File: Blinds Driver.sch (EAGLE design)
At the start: 29 parts

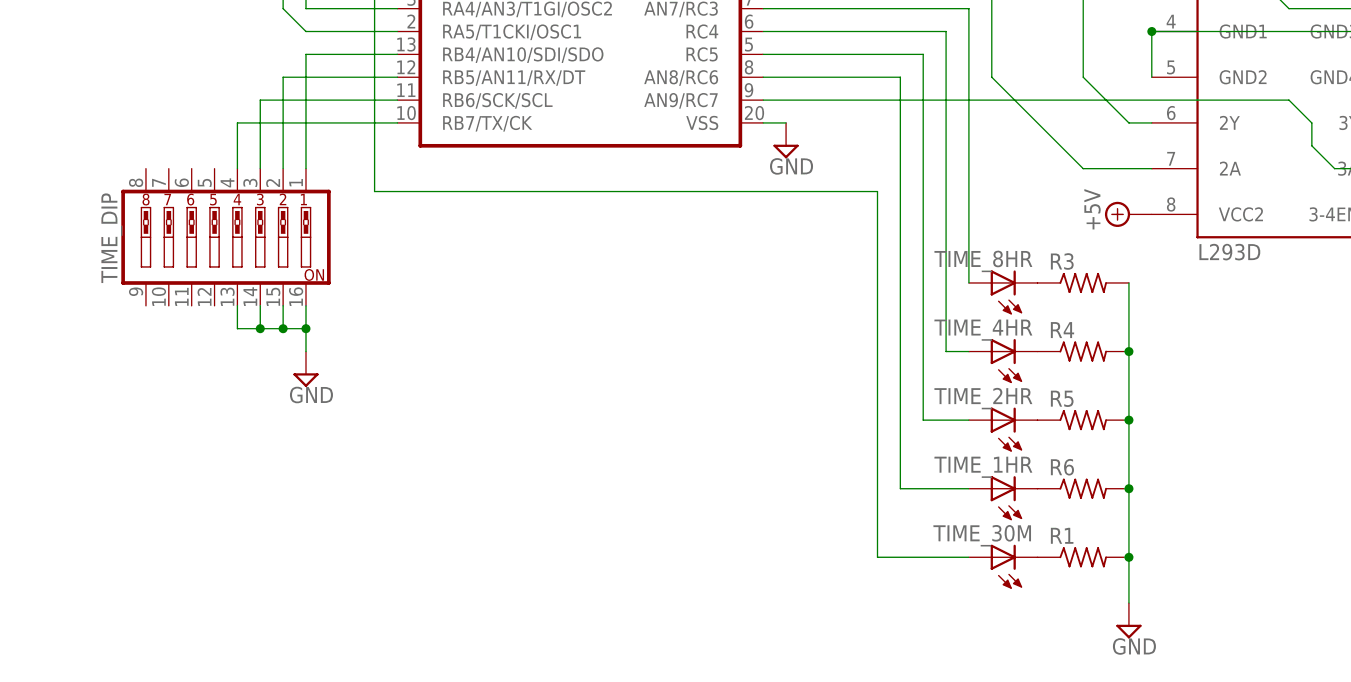
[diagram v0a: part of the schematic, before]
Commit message: Fit into smaller PCB! Use 4-pin DIP
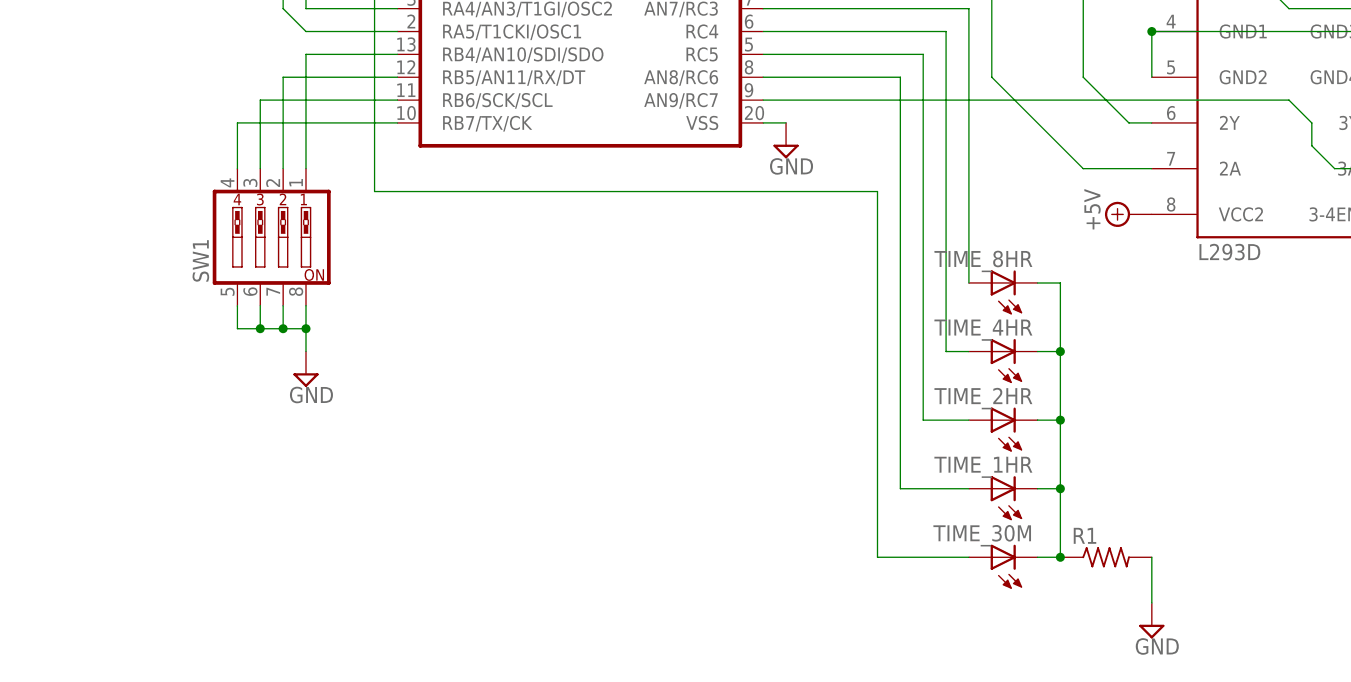
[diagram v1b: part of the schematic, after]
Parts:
- removed R3, R4, R5, R6: (no value), resistor:R-US_0207/10
- removed TIME_DIP: (no value), special:SW_DIP-8
- added SW1: (no value), special:SW_DIP-4
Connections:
- removed net N$15: R4.1, TIME_4HR.C
- removed net N$16: R5.1, TIME_2HR.C
- removed net N$17: R6.1, TIME_1HR.C
- removed net N$23: R1.1, TIME_30M.C
- net GND: now also SW1.5, SW1.6, SW1.7, SW1.8; no longer R3.2, R4.2, R5.2, R6.2, TIME_DIP.13, TIME_DIP.14, TIME_DIP.15, TIME_DIP.16
- net N$14: now also R1.1, TIME_1HR.C, TIME_2HR.C, TIME_30M.C, TIME_4HR.C; no longer R3.1
- net N$4: now also SW1.1; no longer TIME_DIP.1
- net N$5: now also SW1.2; no longer TIME_DIP.2
- net N$7: now also SW1.3; no longer TIME_DIP.3
- net N$9: now also SW1.4; no longer TIME_DIP.4
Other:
- moved on the sheet: R1
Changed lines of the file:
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@@
 <part name="TIME_2HR" library="led" deviceset="LED" device="5MM"/>
 <part name="TIME_1HR" library="led" deviceset="LED" device="5MM"/>
-<part name="R3" library="resistor" deviceset="R-US_" device="0207/10"/>
-<part name="R4" library="resistor" deviceset="R-US_" device="0207/10"/>
-<part name="R5" library="resistor" deviceset="R-US_" device="0207/10"/>
-<part name="R6" library="resistor" deviceset="R-US_" device="0207/10"/>
 <part name="R7" library="resistor" deviceset="R-US_" device="0207/10"/>
 <part name="R8" library="resistor" deviceset="R-US_" device="0207/10"/>
@@
 <part name="TIME_30M" library="led" deviceset="LED" device="5MM"/>
 <part name="R1" library="resistor" deviceset="R-US_" device="0207/10"/>
-<part name="TIME_DIP" library="special" deviceset="SW_DIP-8" device=""/>
 <part name="SUPPLY12" library="supply2" deviceset="GND" device=""/>
 <part name="D1" library="diode" deviceset="1N4004" device=""/>
@@
 <part name="SUPPLY21" library="supply2" deviceset="+12V" device=""/>
 <part name="MOTOR_OUT" library="linear" deviceset="78*" device="T" technology="05"/>
+<part name="SW1" library="special" deviceset="SW_DIP-4" device=""/>
 </parts>
 <sheets>
@@
 <instance part="TIME_2HR" gate="G$1" x="25.4" y="17.78" rot="R90"/>
 <instance part="TIME_1HR" gate="G$1" x="25.4" y="10.16" rot="R90"/>
-<instance part="R3" gate="G$1" x="35.56" y="33.02"/>
-<instance part="R4" gate="G$1" x="35.56" y="25.4"/>
-<instance part="R5" gate="G$1" x="35.56" y="17.78"/>
-<instance part="R6" gate="G$1" x="35.56" y="10.16"/>
 <instance part="R7" gate="G$1" x="73.66" y="33.02" rot="R270"/>
 <instance part="R8" gate="G$1" x="38.1" y="78.74"/>
-<instance part="SUPPLY11" gate="GND" x="40.64" y="-5.08"/>
+<instance part="SUPPLY11" gate="GND" x="43.18" y="-5.08"/>
 <instance part="ADDSMALLTIME" gate="1" x="-66.04" y="116.84" rot="R270"/>
 <instance part="ADDLARGETIME" gate="1" x="-66.04" y="104.14" rot="R270"/>
@@
 <instance part="SUPPLY13" gate="GND" x="-78.74" y="116.84" rot="R270"/>
 <instance part="TIME_30M" gate="G$1" x="25.4" y="2.54" rot="R90"/>
-<instance part="R1" gate="G$1" x="35.56" y="2.54"/>
-<instance part="TIME_DIP" gate="A" x="-60.96" y="38.1" rot="R90"/>
+<instance part="R1" gate="G$1" x="38.1" y="2.54"/>
 <instance part="SUPPLY12" gate="GND" x="-50.8" y="22.86"/>
 <instance part="D1" gate="1" x="99.06" y="76.2" rot="R270"/>
@@
 <instance part="SUPPLY21" gate="+12V" x="116.84" y="27.94" rot="R180"/>
 <instance part="MOTOR_OUT" gate="A1" x="137.16" y="55.88" rot="R90"/>
+<instance part="SW1" gate="A" x="-55.88" y="38.1" rot="R90"/>
 </instances>
 <busses>
@@
 </segment>
 <segment>
-<pinref part="R3" gate="G$1" pin="2"/>
-<pinref part="R4" gate="G$1" pin="2"/>
-<wire x1="40.64" y1="33.02" x2="40.64" y2="25.4" width="0.1524" layer="91"/>
-<pinref part="R5" gate="G$1" pin="2"/>
-<wire x1="40.64" y1="25.4" x2="40.64" y2="17.78" width="0.1524" layer="91"/>
-<pinref part="R6" gate="G$1" pin="2"/>
-<wire x1="40.64" y1="17.78" x2="40.64" y2="10.16" width="0.1524" layer="91"/>
-<wire x1="40.64" y1="10.16" x2="40.64" y2="2.54" width="0.1524" layer="91"/>
 <pinref part="SUPPLY11" gate="GND" pin="GND"/>
 <pinref part="R1" gate="G$1" pin="2"/>
-<wire x1="40.64" y1="2.54" x2="40.64" y2="-2.54" width="0.1524" layer="91"/>
-<junction x="40.64" y="2.54"/>
-<junction x="40.64" y="10.16"/>
-<junction x="40.64" y="17.78"/>
-<junction x="40.64" y="25.4"/>
+<wire x1="43.18" y1="2.54" x2="43.18" y2="-2.54" width="0.1524" layer="91"/>
 </segment>
 <segment>
@@
 <segment>
 <pinref part="SUPPLY12" gate="GND" pin="GND"/>
-<pinref part="TIME_DIP" gate="A" pin="16"/>
 <wire x1="-50.8" y1="25.4" x2="-50.8" y2="27.94" width="0.1524" layer="91"/>
-<pinref part="TIME_DIP" gate="A" pin="15"/>
 <wire x1="-50.8" y1="27.94" x2="-50.8" y2="30.48" width="0.1524" layer="91"/>
 <wire x1="-53.34" y1="30.48" x2="-53.34" y2="27.94" width="0.1524" layer="91"/>
 <wire x1="-53.34" y1="27.94" x2="-50.8" y2="27.94" width="0.1524" layer="91"/>
-<pinref part="TIME_DIP" gate="A" pin="14"/>
 <wire x1="-55.88" y1="30.48" x2="-55.88" y2="27.94" width="0.1524" layer="91"/>
 <wire x1="-55.88" y1="27.94" x2="-53.34" y2="27.94" width="0.1524" layer="91"/>
-<pinref part="TIME_DIP" gate="A" pin="13"/>
 <wire x1="-58.42" y1="30.48" x2="-58.42" y2="27.94" width="0.1524" layer="91"/>
 <wire x1="-58.42" y1="27.94" x2="-55.88" y2="27.94" width="0.1524" layer="91"/>
@@
 <junction x="-53.34" y="27.94"/>
 <junction x="-55.88" y="27.94"/>
+<pinref part="SW1" gate="A" pin="5"/>
+<pinref part="SW1" gate="A" pin="6"/>
+<pinref part="SW1" gate="A" pin="7"/>
+<pinref part="SW1" gate="A" pin="8"/>
 </segment>
 <segment>
@@
 <pinref part="TIME_1HR" gate="G$1" pin="A"/>
 <wire x1="15.24" y1="10.16" x2="22.86" y2="10.16" width="0.1524" layer="91"/>
-</segment>
-</net>
-<net name="N$14" class="0">
-<segment>
-<pinref part="TIME_8HR" gate="G$1" pin="C"/>
-<pinref part="R3" gate="G$1" pin="1"/>
-</segment>
-</net>
-<net name="N$15" class="0">
-<segment>
-<pinref part="TIME_4HR" gate="G$1" pin="C"/>
-<pinref part="R4" gate="G$1" pin="1"/>
-</segment>
-</net>
-<net name="N$16" class="0">
-<segment>
-<pinref part="TIME_2HR" gate="G$1" pin="C"/>
-<pinref part="R5" gate="G$1" pin="1"/>
-</segment>
-</net>
-<net name="N$17" class="0">
-<segment>
-<pinref part="TIME_1HR" gate="G$1" pin="C"/>
-<pinref part="R6" gate="G$1" pin="1"/>
 </segment>
 </net>
@@
 </segment>
 </net>
-<net name="N$23" class="0">
-<segment>
-<pinref part="TIME_30M" gate="G$1" pin="C"/>
-<pinref part="R1" gate="G$1" pin="1"/>
-</segment>
-</net>
 <net name="N$24" class="0">
 <segment>
@@
 <net name="N$4" class="0">
 <segment>
-<pinref part="TIME_DIP" gate="A" pin="1"/>
 <wire x1="-50.8" y1="45.72" x2="-50.8" y2="58.42" width="0.1524" layer="91"/>
 <pinref part="CONTROLLER" gate="G$1" pin="RB4/AN10/SDI/SDO"/>
 <wire x1="-50.8" y1="58.42" x2="-40.64" y2="58.42" width="0.1524" layer="91"/>
+<pinref part="SW1" gate="A" pin="1"/>
 </segment>
 </net>
@@
 <pinref part="CONTROLLER" gate="G$1" pin="RB5/AN11/RX/DT"/>
 <wire x1="-40.64" y1="55.88" x2="-53.34" y2="55.88" width="0.1524" layer="91"/>
-<pinref part="TIME_DIP" gate="A" pin="2"/>
 <wire x1="-53.34" y1="55.88" x2="-53.34" y2="45.72" width="0.1524" layer="91"/>
+<pinref part="SW1" gate="A" pin="2"/>
 </segment>
 </net>
@@
 <pinref part="CONTROLLER" gate="G$1" pin="RB6/SCK/SCL"/>
 <wire x1="-40.64" y1="53.34" x2="-55.88" y2="53.34" width="0.1524" layer="91"/>
-<pinref part="TIME_DIP" gate="A" pin="3"/>
 <wire x1="-55.88" y1="53.34" x2="-55.88" y2="45.72" width="0.1524" layer="91"/>
+<pinref part="SW1" gate="A" pin="3"/>
 </segment>
 </net>
@@
 <pinref part="CONTROLLER" gate="G$1" pin="RB7/TX/CK"/>
 <wire x1="-40.64" y1="50.8" x2="-58.42" y2="50.8" width="0.1524" layer="91"/>
-<pinref part="TIME_DIP" gate="A" pin="4"/>
 <wire x1="-58.42" y1="50.8" x2="-58.42" y2="45.72" width="0.1524" layer="91"/>
+<pinref part="SW1" gate="A" pin="4"/>
 </segment>
 </net>
@@
 </segment>
 </net>
+<net name="N$14" class="0">
+<segment>
+<pinref part="TIME_8HR" gate="G$1" pin="C"/>
+<wire x1="30.48" y1="33.02" x2="33.02" y2="33.02" width="0.1524" layer="91"/>
+<wire x1="33.02" y1="33.02" x2="33.02" y2="25.4" width="0.1524" layer="91"/>
+<pinref part="TIME_30M" gate="G$1" pin="C"/>
+<pinref part="R1" gate="G$1" pin="1"/>
+<wire x1="33.02" y1="25.4" x2="33.02" y2="17.78" width="0.1524" layer="91"/>
+<wire x1="33.02" y1="17.78" x2="33.02" y2="10.16" width="0.1524" layer="91"/>
+<wire x1="33.02" y1="10.16" x2="33.02" y2="2.54" width="0.1524" layer="91"/>
+<wire x1="33.02" y1="2.54" x2="30.48" y2="2.54" width="0.1524" layer="91"/>
+<pinref part="TIME_1HR" gate="G$1" pin="C"/>
+<wire x1="30.48" y1="10.16" x2="33.02" y2="10.16" width="0.1524" layer="91"/>
+<pinref part="TIME_2HR" gate="G$1" pin="C"/>
+<wire x1="30.48" y1="17.78" x2="33.02" y2="17.78" width="0.1524" layer="91"/>
+<pinref part="TIME_4HR" gate="G$1" pin="C"/>
+<wire x1="30.48" y1="25.4" x2="33.02" y2="25.4" width="0.1524" layer="91"/>
+<junction x="33.02" y="25.4"/>
+<junction x="33.02" y="17.78"/>
+<junction x="33.02" y="10.16"/>
+<junction x="33.02" y="2.54"/>
+</segment>
+</net>

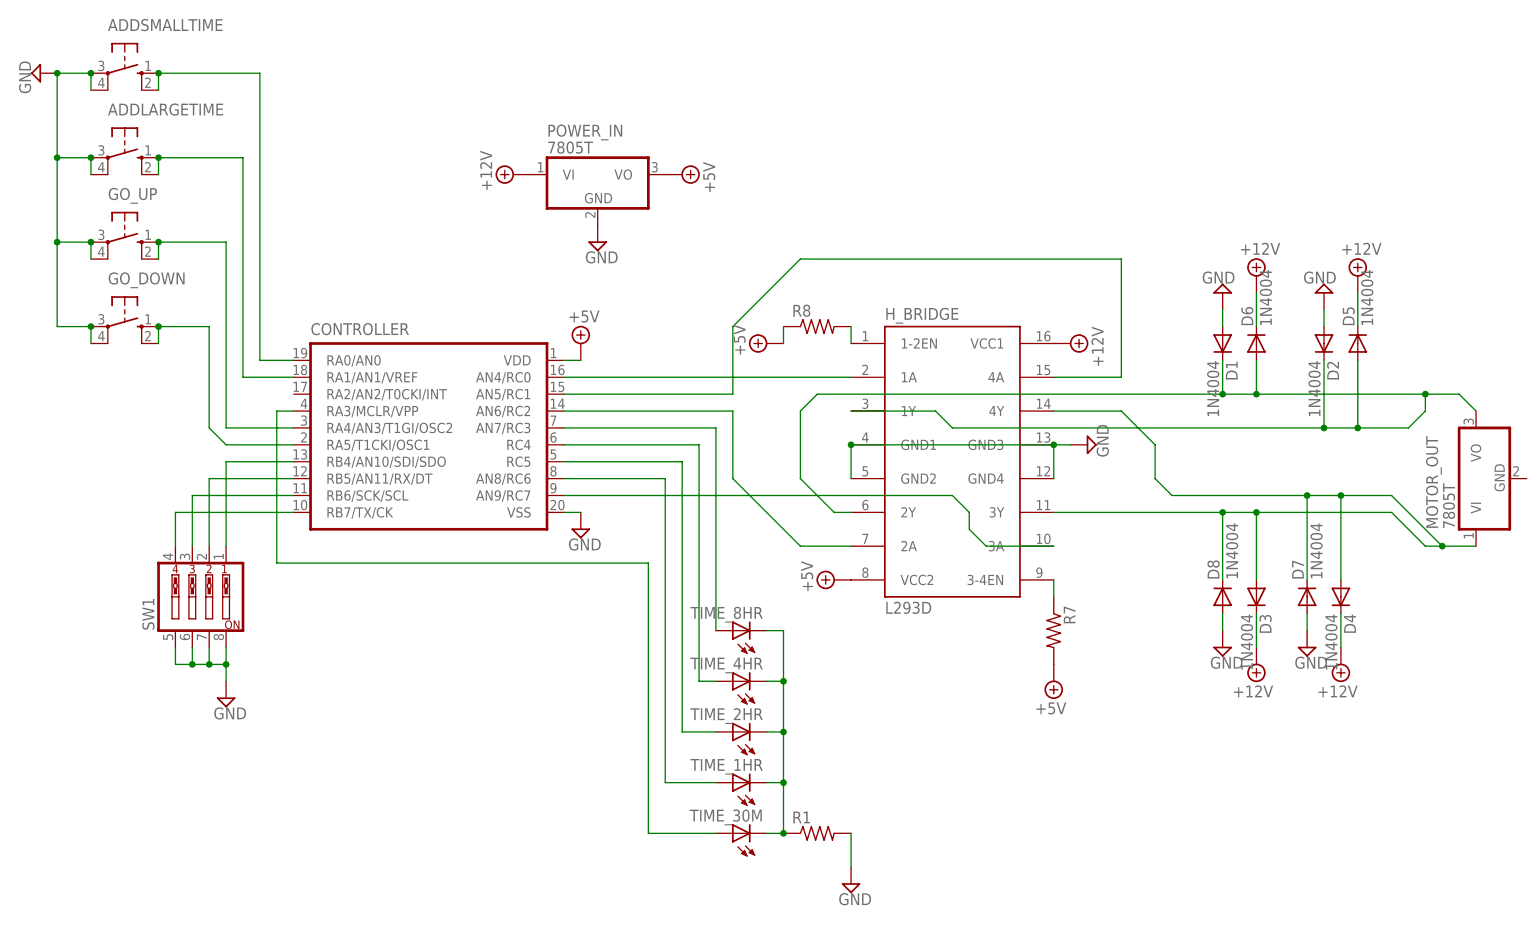
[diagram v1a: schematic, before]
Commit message: 1) Diodes were doubled up 2) Only one half-bridge is needed 3) VCC 2 is +12V, VCC1 is +5V 4) Added 2 bypass capacitors on the power supply lines to stabilize power supply
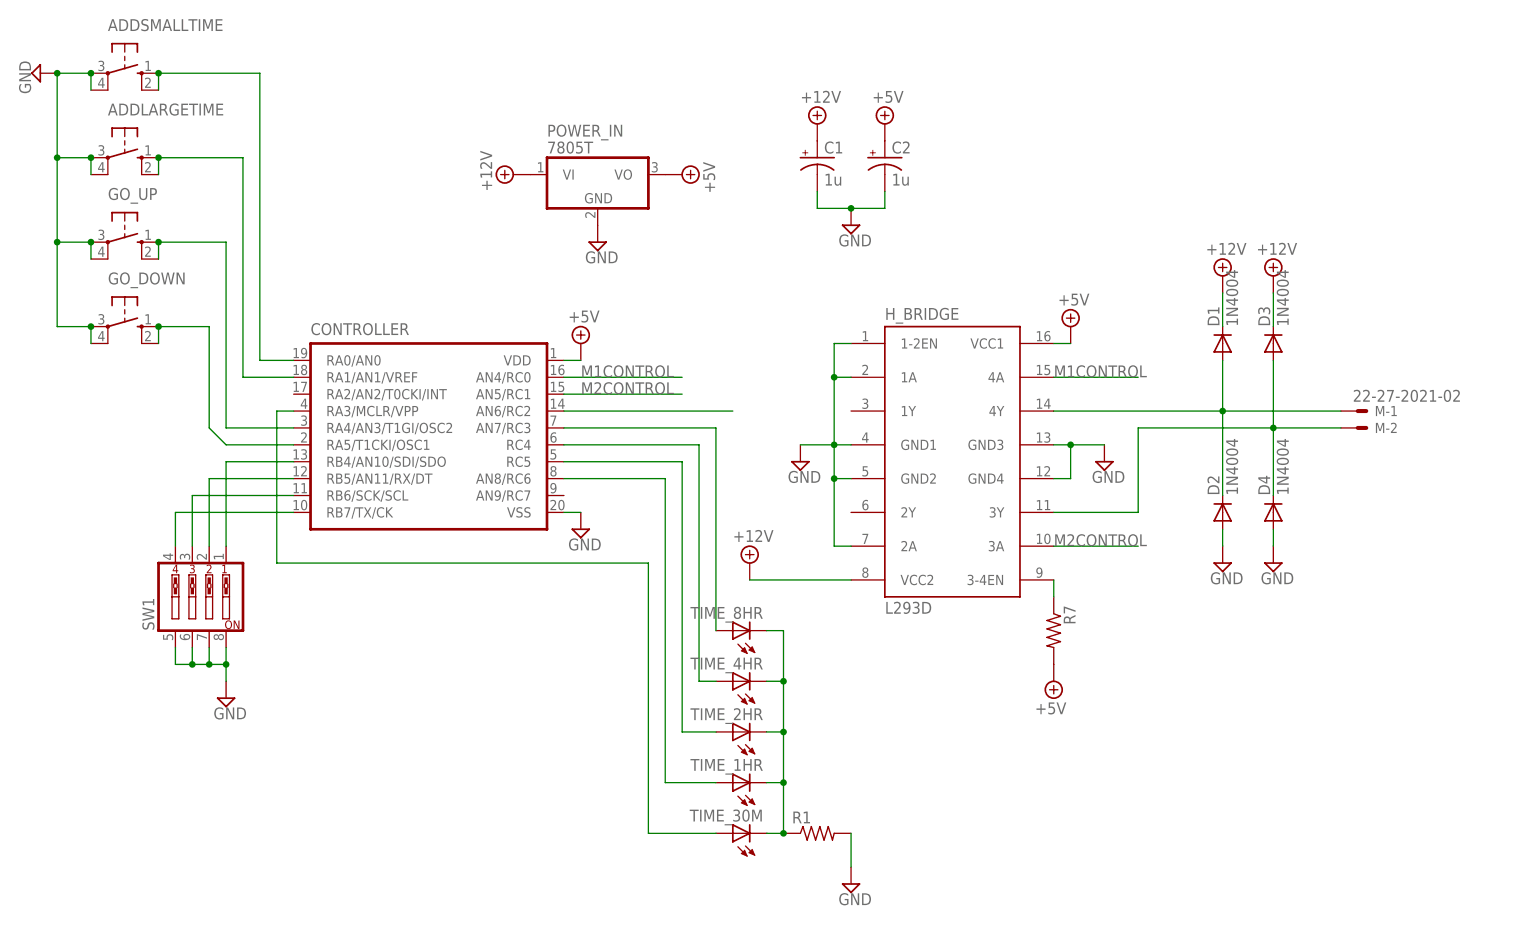
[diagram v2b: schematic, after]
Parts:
- removed D5, D6, D7, D8: 1N4004, diode:1N4004
- removed MOTOR_OUT: 7805T, linear:7805T
- removed R8: (no value), resistor:R-US_0207/10
- added C1, C2: 1u, rcl:CPOL-USE2,5-6E
- added M: 22-27-2021-02, con-molex:22-27-2021-02
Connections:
- removed net N$1: CONTROLLER.AN4/RC0, H_BRIDGE.1A
- removed net N$22: CONTROLLER.AN9/RC7, H_BRIDGE.3A
- removed net N$25: D1.C, D2.C, D5.A, D6.A, H_BRIDGE.1Y, H_BRIDGE.2Y, MOTOR_OUT.VO
- removed net N$28: D3.A, D4.A, D7.C, D8.C, H_BRIDGE.3Y, H_BRIDGE.4Y, MOTOR_OUT.VI
- new net M1CONTROL: CONTROLLER.AN4/RC0, H_BRIDGE.4A
- new net M2CONTROL: CONTROLLER.AN5/RC1, H_BRIDGE.3A
- net +12V: now also C1.+, D1.C, H_BRIDGE.VCC2; no longer D4.C, D5.C, D6.C, H_BRIDGE.VCC1
- net +5V: now also C2.+, H_BRIDGE.VCC1; no longer H_BRIDGE.VCC2, R8.1
- net GND: now also C1.-, C2.-, D4.A, H_BRIDGE.1-2EN, H_BRIDGE.1A, H_BRIDGE.2A; no longer D1.A, D7.A, D8.A
- net N$2: no longer H_BRIDGE.2A
- net N$3: now also D1.A, D2.C, H_BRIDGE.4Y, M-1.S; no longer CONTROLLER.AN5/RC1, H_BRIDGE.4A
- net N$6: now also D3.A, D4.C, H_BRIDGE.3Y, M-2.S; no longer H_BRIDGE.1-2EN, R8.2
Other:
- moved on the sheet: D1, D2, D3, D4
